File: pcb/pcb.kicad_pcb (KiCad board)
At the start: 2 copper layers, 100 x 88.7 mm, 65 parts, among them J1 AudioJack4, J2 USB_C_Receptacle_USB2.0, SW1 Switch, SW10 Switch, SW11 Switch, SW12 Switch, SW13 Switch, SW14 Switch, SW15 Switch, SW16 Switch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

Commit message: new pcb
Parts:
- removed J2: USB_C_Receptacle_USB2.0, zzkeeb:Connector_USB-C-mid-mount-ali-reversible-data
- removed LED1, LED10, LED11, LED12, LED13, LED14, LED15, LED16, LED17, LED18, LED2, LED3, LED4, LED5, LED6, LED7, LED8, LED9: LED_SK6812MINI-E, zzkeeb:LED_SK6812-MINI-E-reversible
- removed SW15, SW16: Switch, zzkeeb:Switch_ChocV1-hotswap-reversible
- removed U3: RollerEncoder_EVQWGD001, zzkeeb:RotaryEncoder_EVQWGD001
- added FiveWay1: 5Way-Tactile_K1-1506DN-01, zzkeeb:Button_5way, F.Cu at (100.9, 111.5)
- added J3: C0, Connector_PinHeader_2.54mm:PinHeader_1x01_P2.54mm_Vertical, F.Cu at (55.5, 84.5)
- added J4: R3, Connector_PinHeader_2.54mm:PinHeader_1x01_P2.54mm_Vertical, F.Cu at (55.5, 88.5)
- added J5: C2, Connector_PinHeader_2.54mm:PinHeader_1x01_P2.54mm_Vertical, F.Cu at (150.0, 106.5)
- added R1: 4.7k, Resistor_SMD:R_1206_3216Metric_Pad1.30x1.75mm_HandSolder, B.Cu at (77.0, 48.5)
- added R2: 4.7k, Resistor_SMD:R_1206_3216Metric_Pad1.30x1.75mm_HandSolder, F.Cu at (77.0, 48.5)
- added USB1: Connector_HRO-TYPE-C-31-M-12, zzkeeb:Connector_HRO-TYPE-C-31-M-12-data, B.Cu at (144.5, 40.5)
- added USB2: Connector_HRO-TYPE-C-31-M-12, zzkeeb:Connector_HRO-TYPE-C-31-M-12-data, F.Cu at (144.5, 40.5)
- D1, D10, D11, D12, D13, D14, D15, D16, D17, D18, D19, D2, D3, D4, D5, D6, D7, D8, D9: footprint zzkeeb:Diode_1N4148-SOD123-reversible-flip3d -> zzkeeb:Diode_1N4148-SOD123-no-label-reversible-flip3d
- J1: value AudioJack4 -> R3; footprint zzkeeb:Connector_TRRS-reversible -> Connector_PinHeader_2.54mm:PinHeader_1x01_P2.54mm_Vertical
- SW1, SW10, SW11, SW12, SW13, SW14, SW2, SW3, SW4, SW5, SW6, SW7, SW8, SW9: footprint zzkeeb:Switch_ChocV1-hotswap-reversible -> zzkeeb:Switch_MX-hotswap-miny-reversible
- SW17, SW18: footprint zzkeeb:Switch_ChocV1-hotswap-reversible -> zzkeeb:Switch_KS-miny-reversible-hotswap-south
- moved J1 64.0 mm to (150.0, 110.5), turned to 0 degrees
- moved D15 54.2 mm to (117.0, 99.5), turned to 0 degrees
- moved D19 27.1 mm to (117.0, 102.5), turned to 0 degrees
- moved D13 19.0 mm to (121.5, 84.1), turned to 0 degrees
- moved D8 18.0 mm to (121.5, 68.1), turned to 0 degrees
- moved D16 17.8 mm to (108.5, 99.5), turned to 0 degrees
- moved H3 17.8 mm to (64.5, 102.0)
- moved D14 17.2 mm to (140.5, 86.1), turned to 0 degrees
- moved D3 17.0 mm to (121.5, 52.1), turned to 0 degrees
- moved RE1 16.4 mm to (100.5, 111.5)
- moved D9 16.2 mm to (140.5, 70.1), turned to 0 degrees
- moved D12 15.4 mm to (102.5, 79.1), turned to 0 degrees
- moved D11 15.4 mm to (83.5, 84.1), turned to 0 degrees
- moved D18 15.3 mm to (108.5, 96.5), turned to 0 degrees
- moved D4 15.2 mm to (140.5, 54.1), turned to 0 degrees
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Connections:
- D15 pad 2: Net-(D15-Pad2) -> Net-(D15-A)
- U1 pad 19: LED -> unconnected-(U1-28-Pad19)
- U2 pad 19: LED -> unconnected-(U2-28-Pad19)
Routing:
- net VCC: track 635.8 -> 138.4 mm, vias 20 -> 2
- net row4: track 0.00 -> 108.5 mm, vias 0 -> 2
- net LED: track 67.4 -> 0.00 mm, vias 2 -> 0
- net RX: track 171.9 -> 120.3 mm, vias 6 -> 2
- net row3: track 175.1 -> 130.5 mm, vias 6 -> 4
- net Net-(LED15-Pad4): track 44.0 -> 0.00 mm, vias 2 -> 0
- net TX: track 159.1 -> 116.1 mm, vias 5 -> 2
- net Net-(D15-A): track 0.00 -> 43.1 mm, vias 0 -> 2
- net Net-(LED14-Pad2): track 39.7 -> 0.00 mm, vias 2 -> 0
- net Net-(LED1-Pad2): track 38.8 -> 0.00 mm, vias 2 -> 0
- net Net-(LED11-Pad2): track 37.3 -> 0.00 mm, vias 2 -> 0
- net hand: track 0.00 -> 36.9 mm, vias 0 -> 1
- net Net-(LED4-Pad2): track 34.5 -> 0.00 mm, vias 2 -> 0
- net col1: track 177.5 -> 143.2 mm, vias 4 -> 6
- net Net-(LED10-Pad2): track 34.4 -> 0.00 mm, vias 2 -> 0
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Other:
- board size 100 x 88.7 mm -> 100 x 82.5 mm

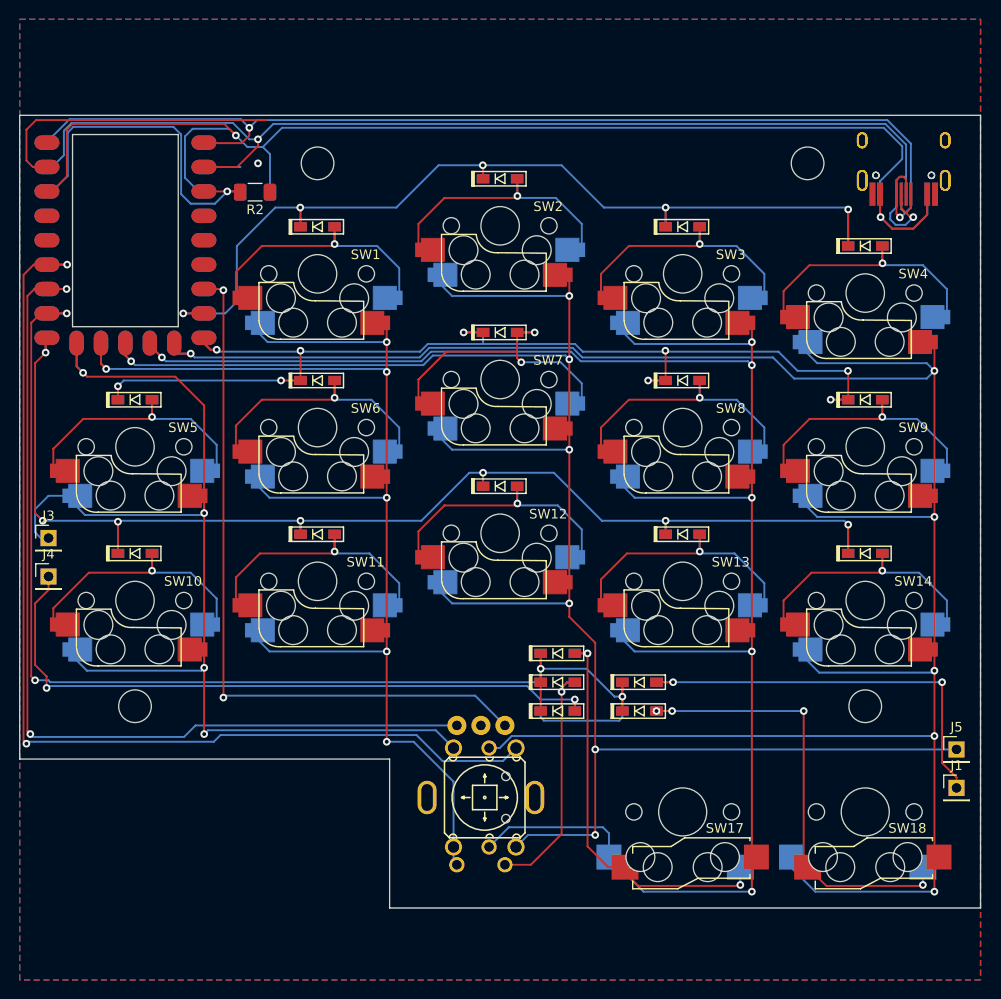
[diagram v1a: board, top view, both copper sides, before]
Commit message: improve labels
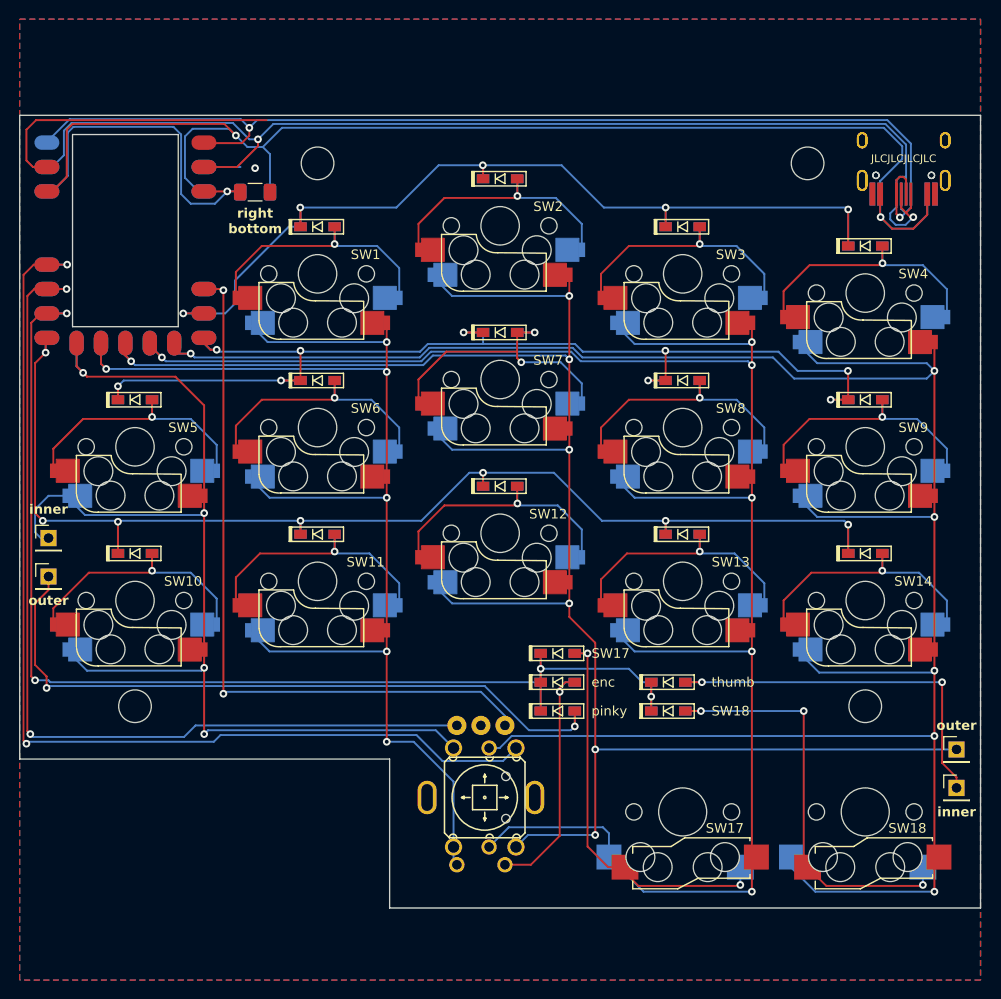
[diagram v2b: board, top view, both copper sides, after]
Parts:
- moved D15 3.00 mm to (120.0, 99.5)
- moved D19 3.00 mm to (120.0, 102.5)
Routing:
- net row3: track 130.5 -> 125.8 mm
- net Net-(D19-A): track 48.2 -> 45.2 mm, vias 4 -> 3
- net Net-(D15-A): track 43.1 -> 40.1 mm
- net row0: track 102.2 -> 99.4 mm
- net Net-(D17-A): track 70.7 -> 73.0 mm
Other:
- board text added: "JLCJLCJLCJLC"
- board text added: "SW17"
- board text added: "SW18"
- board text added: "enc"
- board text added: "inner"
- board text added: "left bottom"
- board text added: "miny"
- board text added: "outer"
- board text added: "pinky"
- board text added: "right bottom"
- board text added: "thumb"
- board text added: "v0.1"

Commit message: rounded tracks
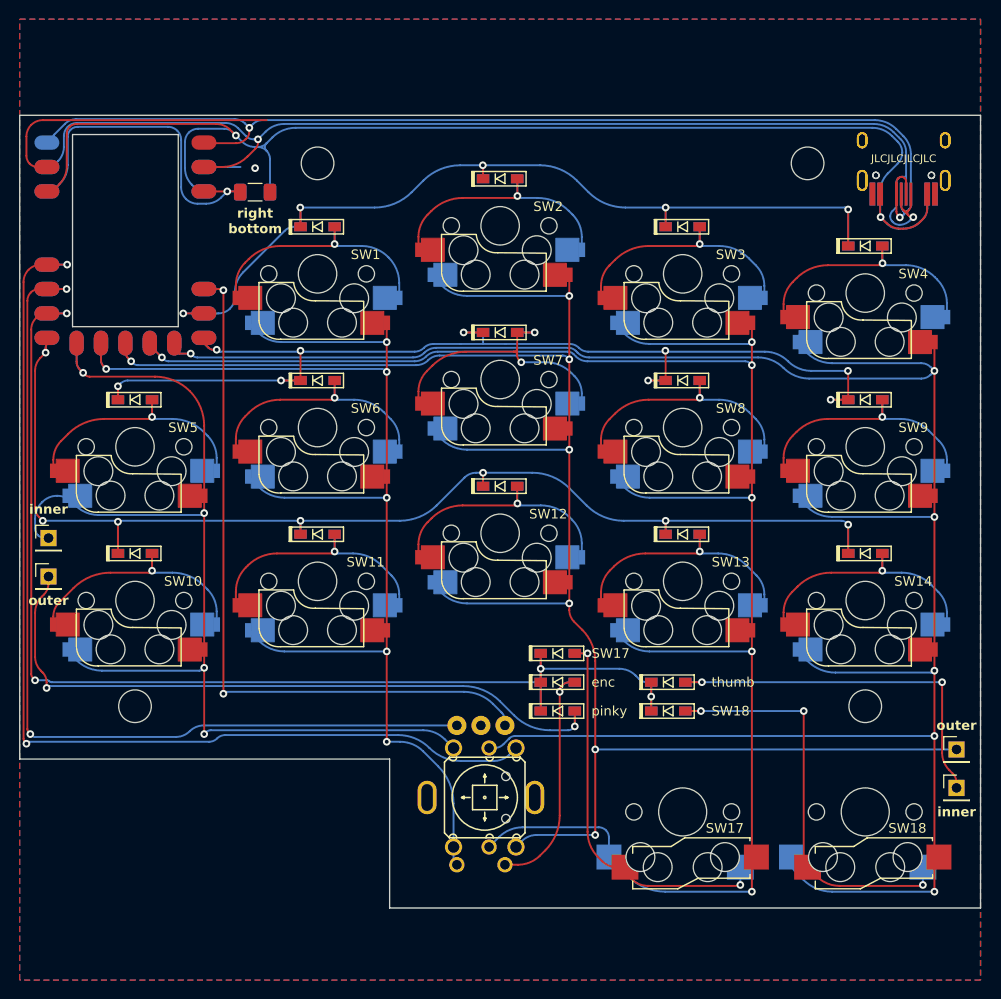
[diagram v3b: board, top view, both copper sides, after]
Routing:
- net col4: track 255.0 -> 251.8 mm
- net col3: track 205.7 -> 203.9 mm
- net col0: track 121.5 -> 119.9 mm
- net row0: track 99.4 -> 98.0 mm
- net col2: track 203.4 -> 202.2 mm
- net row2: track 132.6 -> 131.4 mm
- net col1: track 143.2 -> 142.1 mm
- net Net-(D17-A): track 73.0 -> 72.1 mm
- net row4: track 108.5 -> 107.6 mm
- net Net-(D5-A): track 27.8 -> 27.0 mm
- net Net-(D2-A): track 28.0 -> 27.2 mm
- net Net-(D4-A): track 28.1 -> 27.4 mm
- net Net-(D12-A): track 28.1 -> 27.4 mm
- net Net-(D1-A): track 28.8 -> 28.1 mm
- net Net-(D10-A): track 27.4 -> 26.6 mm
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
